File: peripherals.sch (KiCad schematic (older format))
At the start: 26 parts, among them J5 PIO Header, J6 Port A, J7 Port A, J8 IDE, U6 Z84C2010AEG, U7 Z84C4310AEG, U8 Z84C3010AEG

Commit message: Renamed to SMC-80
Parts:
- R10, R11, R12, R9: symbol THS-80-rescue:R_Small-Device-sbc_z80-rescue -> SMC-80-rescue:R_Small-Device-sbc_z80-rescue
- U6: symbol THS-80:Z84C2010AEG -> SMC-80:Z84C2010AEG
- U7: symbol THS-80:Z84C4310AEG -> SMC-80:Z84C4310AEG
- U8: symbol THS-80:Z84C3010AEG -> SMC-80:Z84C3010AEG
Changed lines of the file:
@@
 encoding utf-8
 Sheet 4 6
-Title "THS-80"
+Title "SMC-80"
 Date "2019-08-15"
 Rev "1.0"
@@
 $EndComp
 $Comp
-L THS-80:Z84C4310AEG U7
+L SMC-80:Z84C4310AEG U7
 U 1 1 5DAA1781
 P 2450 2100
@@
 $EndComp
 $Comp
-L THS-80:Z84C2010AEG U6
+L SMC-80:Z84C2010AEG U6
 U 1 1 5E20570F
 P 2350 5750
@@
 $EndComp
 $Comp
-L THS-80:Z84C3010AEG U8
+L SMC-80:Z84C3010AEG U8
 U 1 1 5E4FBAAF
 P 8450 2050
@@
 $EndComp
 $Comp
-L THS-80-rescue:GND-power-sbc_z80-rescue-THS-80-rescue-de10-lite-ram-rom-rescue #PWR?
+L SMC-80-rescue:GND-power-sbc_z80-rescue-SMC-80-rescue-de10-lite-ram-rom-rescue #PWR?
 U 1 1 5DAC563D
 P 10700 5425
@@
 CLK_B
 $Comp
-L THS-80-rescue:R_Small-Device-sbc_z80-rescue R?
+L SMC-80-rescue:R_Small-Device-sbc_z80-rescue R?
 U 1 1 5DBFA8AC
 P 4675 2525
@@
 $EndComp
 $Comp
-L THS-80-rescue:GND-power-sbc_z80-rescue #PWR?
+L SMC-80-rescue:GND-power-sbc_z80-rescue #PWR?
 U 1 1 5DBFA8B2
 P 5000 2750
@@
 $EndComp
 $Comp
-L THS-80-rescue:R_Small-Device-sbc_z80-rescue R?
+L SMC-80-rescue:R_Small-Device-sbc_z80-rescue R?
 U 1 1 5DBFA8C2
 P 4850 3450
@@
 $EndComp
 $Comp
-L THS-80-rescue:R_Small-Device-sbc_z80-rescue R?
+L SMC-80-rescue:R_Small-Device-sbc_z80-rescue R?
 U 1 1 5E05EC3F
 P 4675 925
@@
 $EndComp
 $Comp
-L THS-80-rescue:R_Small-Device-sbc_z80-rescue R?
+L SMC-80-rescue:R_Small-Device-sbc_z80-rescue R?
 U 1 1 5E05EC55
 P 4850 1850
@@
 $EndComp
 $Comp
-L THS-80-rescue:GND-power-sbc_z80-rescue #PWR?
+L SMC-80-rescue:GND-power-sbc_z80-rescue #PWR?
 U 1 1 5E05EC45
 P 5000 1150

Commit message: Routing finished
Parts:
- renumbered C20 to C17, C21 to C18, C22 to C19, C23 to C20, JP2 to JP1, JP3 to JP2, JP4 to JP3, R11 to R10, R12 to R11, R13 to R12, R14 to R13, R15 to R14, R16 to R15, R8 to R7, R9 to R8, R10 to R9, U6 to U4, U7 to U5, U8 to U6

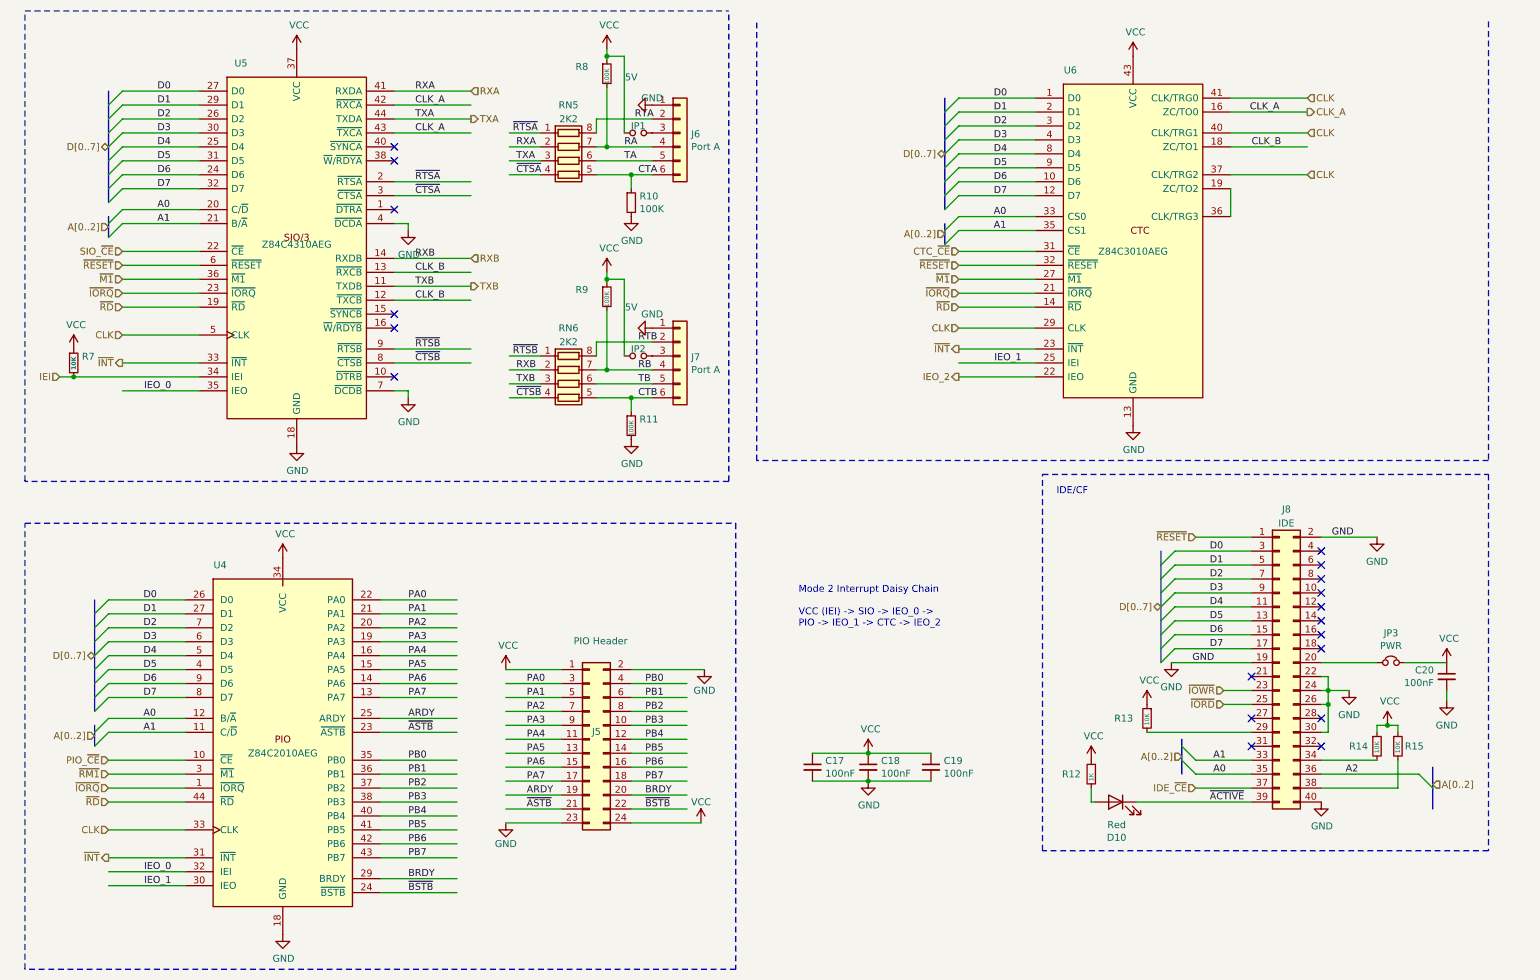
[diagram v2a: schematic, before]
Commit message: reorganized sheets, added SIO clk select
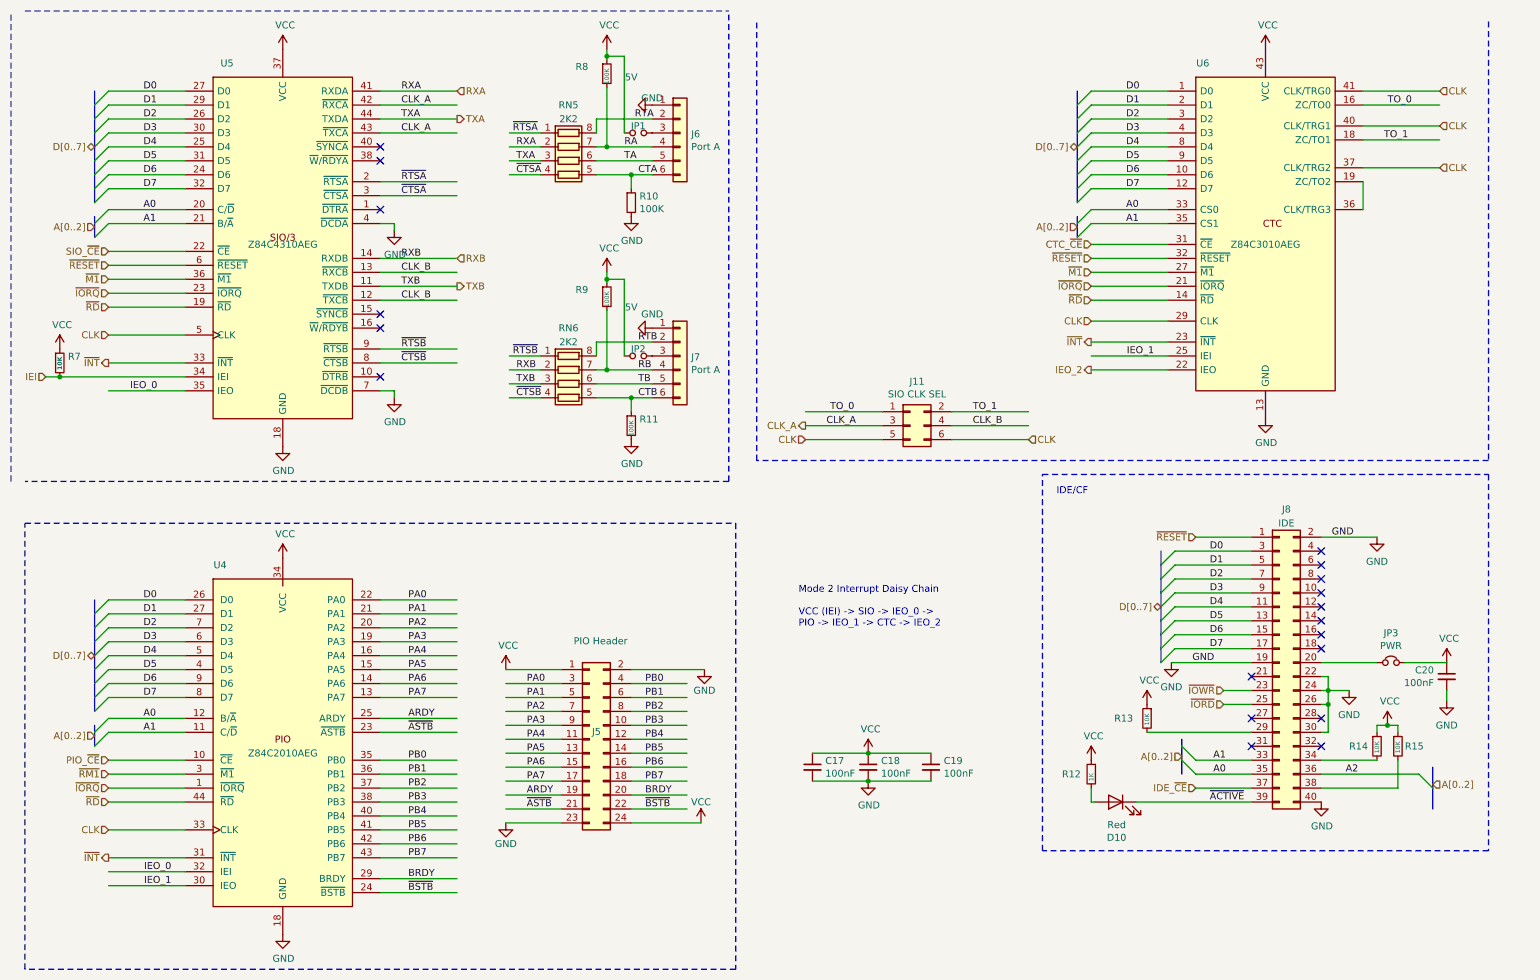
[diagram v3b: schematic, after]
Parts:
- added J11: SIO CLK SEL, Connector_PinHeader_2.54mm:PinHeader_2x03_P2.54mm_Vertical, symbol Connector_Generic:Conn_02x03_Odd_Even
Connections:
- net labels added: TO_0, TO_1
- wire segments 200 -> 206
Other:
- moved on the sheet: R7, U5, U6

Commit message: remove old files, added jtag pullup
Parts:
- renumbered J11 to J8, J8 to J9, JP1 to JP2, JP2 to JP3, JP3 to JP4, R8 to R10, R9 to R11, R10 to R12, R11 to R13, R12 to R14, R13 to R15, R14 to R16, R15 to R17, R7 to R9, U4 to U6, U6 to U7
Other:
- note added: "Mode 2 Interrupt Daisy Chain\n\nVCC (IEI) -> SIO -> IEO_0 -> \nCTC -> IEO_1 -> PIO -> IEO_2"
- note removed: "Mode 2 Interrupt Daisy Chain\n\nVCC (IEI) -> SIO -> IEO_0 -> \nPIO -> IEO_1 -> CTC -> IEO_2"
